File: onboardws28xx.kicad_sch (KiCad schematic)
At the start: 65 parts

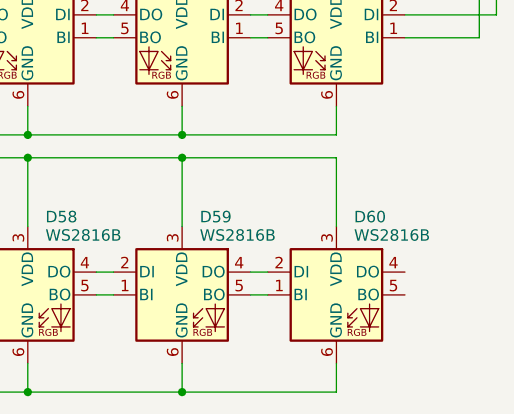
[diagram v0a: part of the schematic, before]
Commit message: schematic DRC now ok
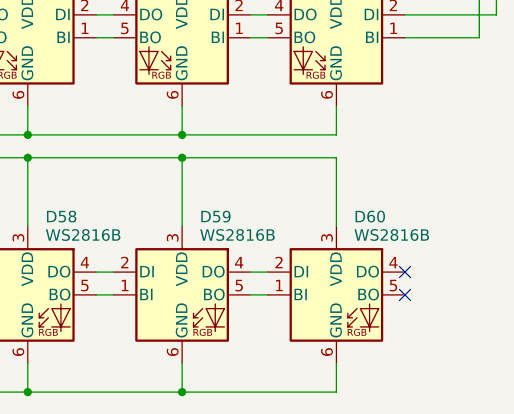
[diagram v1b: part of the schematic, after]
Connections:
- no-connect marks 0 -> 2
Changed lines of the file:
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@@
   (junction (at 40.005 132.715) (diameter 0) (color 0 0 0 0)
   )
+  (no_connect (at 265.43 147.955))
+  (no_connect (at 265.43 150.495))
   (wire (pts (xy 265.43 33.655) (xy 275.59 33.655))
     (stroke (width 0) (type default))

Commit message: Populate module/purpose fields for BOM, generate iBOM
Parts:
- C5: Module (none) -> Onboard_LED; Purpose (none) -> Bulk Cap LEDs
- D1, D10, D11, D12, D13, D14, D15, D16, D17, D18, D19, D2, D20, D21, D22, D23, D24, D25, D26, D27, D28, D29, D3, D30, D31, D32, D33, D34, D35, D36, D37, D38, D39, D4, D40, D41, D42, D43, D44, D45, D46, D47, D48, D49, D5, D50, D51, D52, D53, D54, D55, D56, D57, D58, D59, D6, D60, D7, D8, D9: Module (none) -> Onboard_LED; Purpose (none) -> On Board RGB LED display; Vendor (none) -> LCSC
